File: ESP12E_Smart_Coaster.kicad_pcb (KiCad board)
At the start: 2 copper layers, 110.7 x 110.7 mm, 48 parts, among them J1 GPIO_Header, J2 SPI_Header, J3 MLX90614 Temp Sensor, J4 Programming_header, Q1 SI2302, SW1 SW_SPDT, SW2 SW_Push, U1 T6845C_Module, U2 AMS1117-3.3, U3 ESP-12E

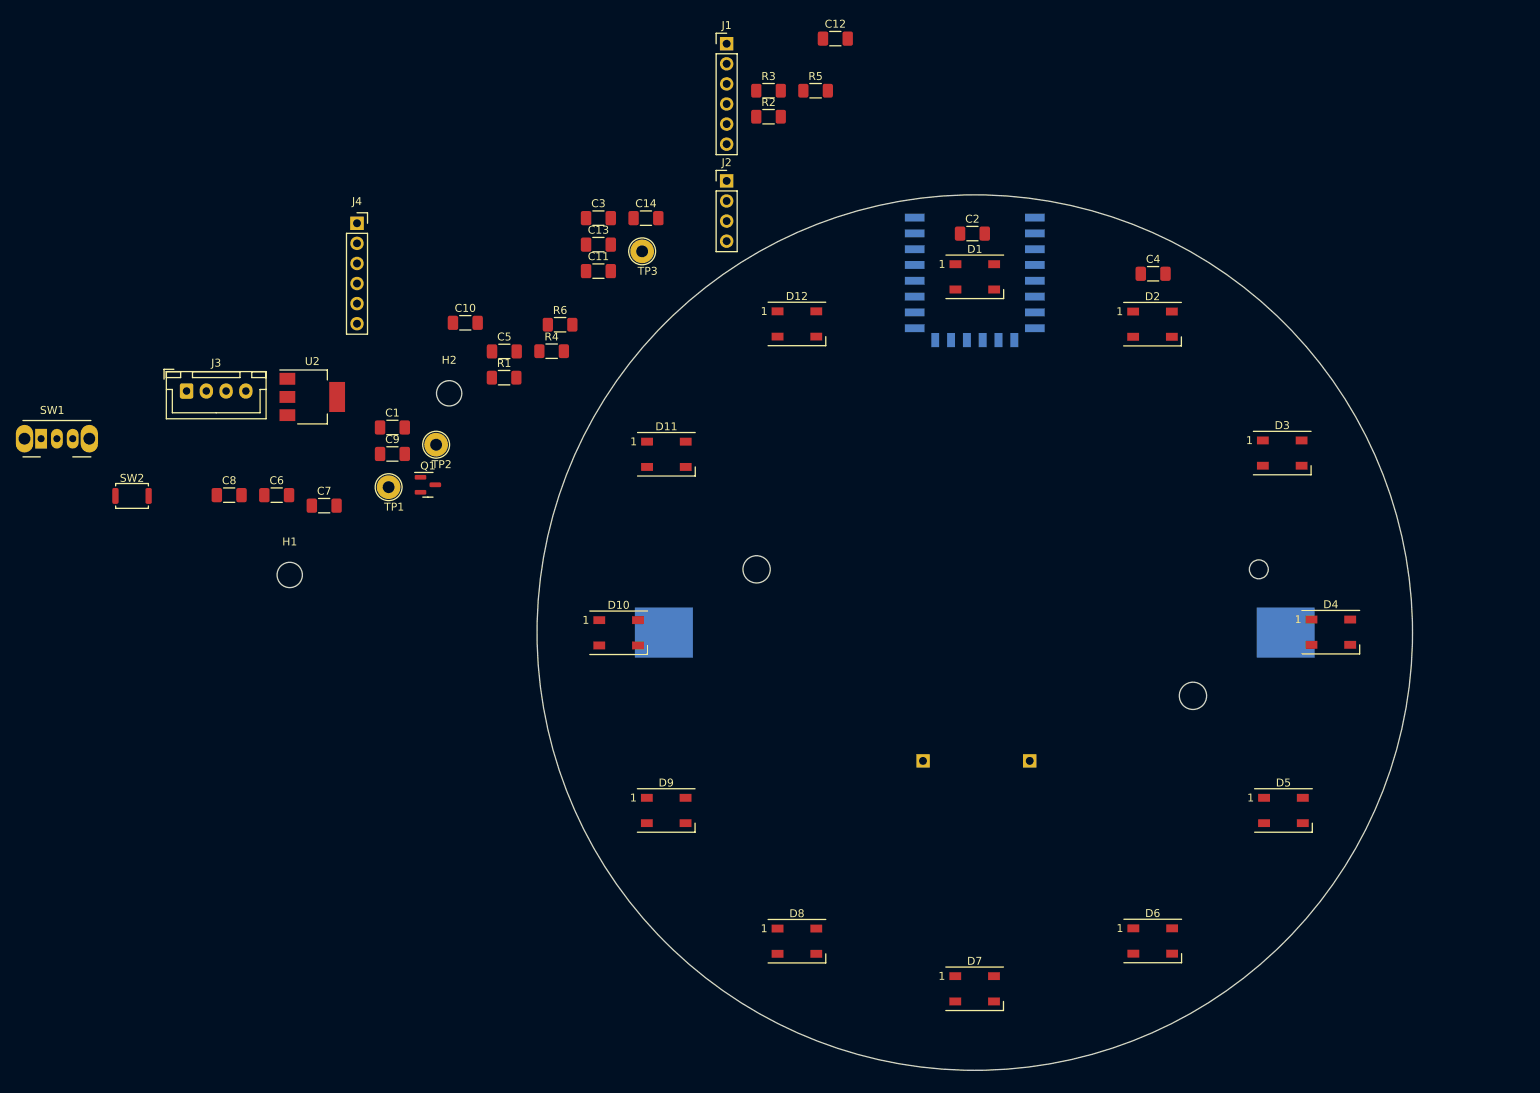
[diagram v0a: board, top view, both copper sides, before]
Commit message: re-arrange components but not completely done
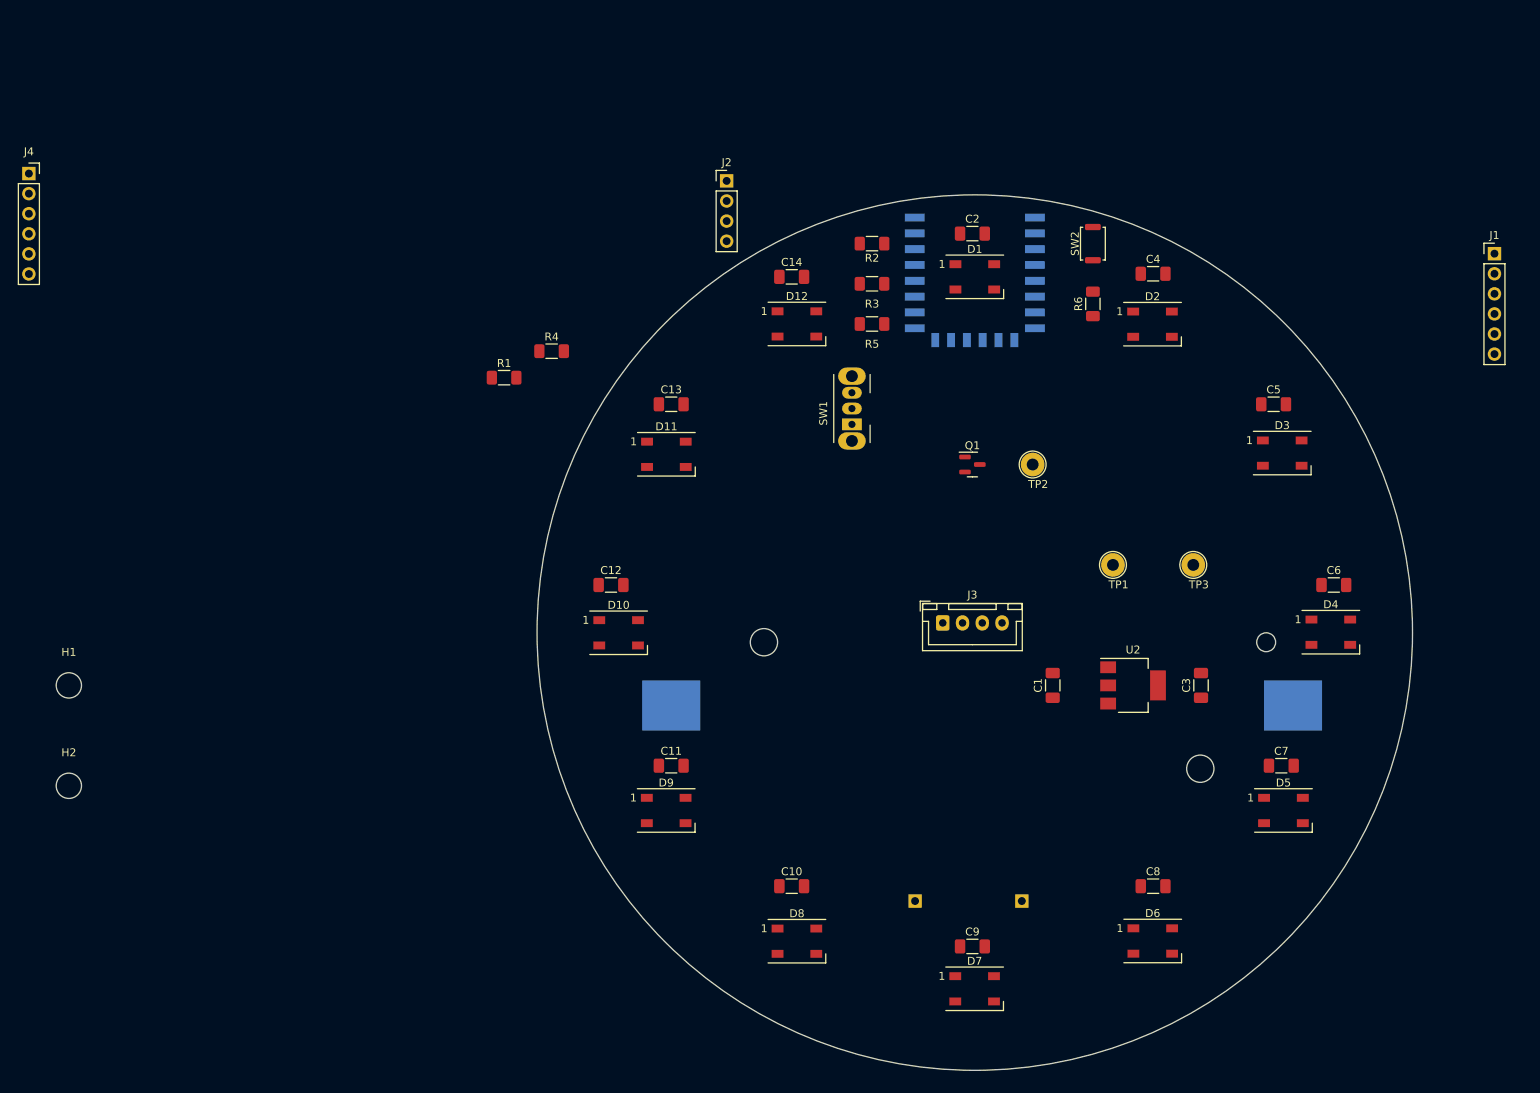
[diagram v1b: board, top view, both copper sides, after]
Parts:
- moved C6 134.2 mm to (185.4, 94.0)
- moved C8 126.9 mm to (162.6, 132.1)
- moved SW2 125.7 mm to (154.9, 50.8), turned to 90 degrees
- moved C7 125.5 mm to (178.8, 116.8)
- moved U2 110.1 mm to (160.0, 106.7)
- moved SW1 102.6 mm to (124.5, 73.7), turned to 90 degrees
- moved J1 100.7 mm to (205.7, 52.1)
- moved J3 100.1 mm to (135.9, 98.8)
- moved C5 97.5 mm to (177.8, 71.1)
- moved C3 96.5 mm to (168.6, 106.7), turned to 90 degrees
- moved C9 96.2 mm to (139.7, 139.7)
- moved TP1 92.2 mm to (157.5, 91.4)
- moved C1 89.7 mm to (149.9, 106.7), turned to 90 degrees
- moved C10 82.4 mm to (116.8, 132.1)
- moved TP3 80.2 mm to (167.6, 91.4)
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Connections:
- R3 pad 1: RESET -> (no net)
- R3 pad 2: GPIO2 -> (no net)

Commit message: Started PCB routing
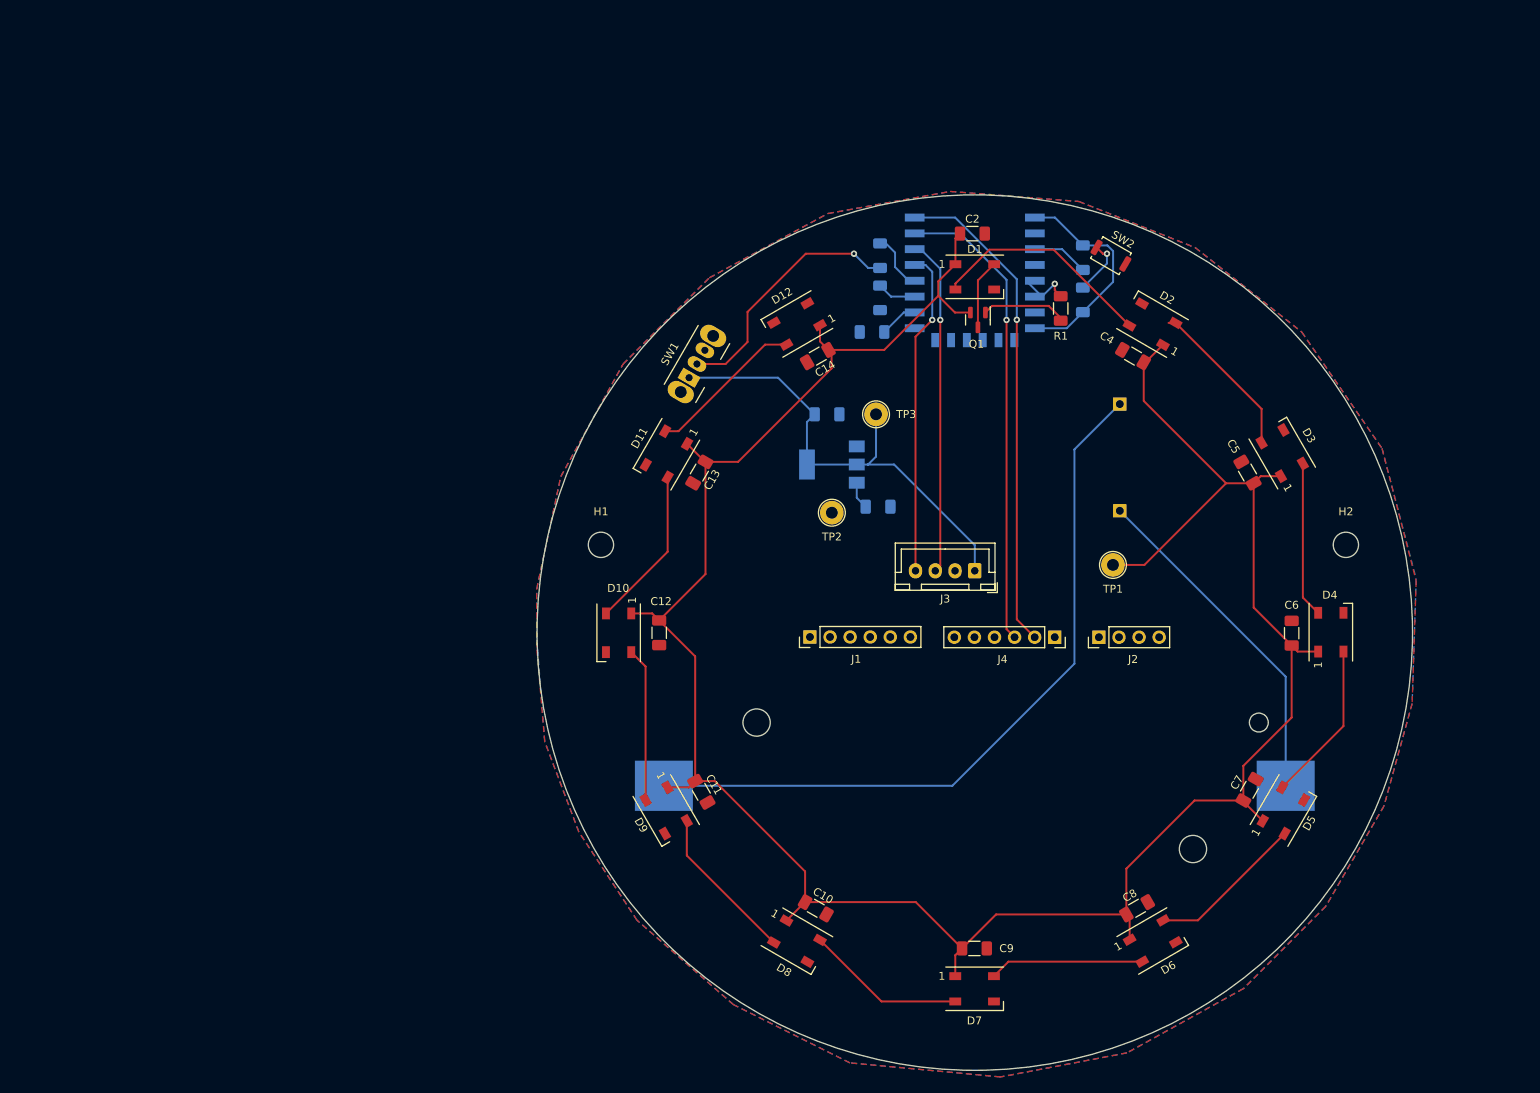
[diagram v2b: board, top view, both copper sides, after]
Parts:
- C1, C3, R2, R3, R4, R5, R6, U2: moved to B.Cu
- TP2: value 5V -> GND
- moved H2 164.4 mm to (186.9, 88.9)
- moved J4 142.4 mm to (150.1, 100.6), turned to -90 degrees
- moved J1 99.2 mm to (119.2, 100.6), turned to 90 degrees
- moved J2 74.5 mm to (155.7, 100.6), turned to 90 degrees
- moved R1 70.9 mm to (150.9, 59.0), turned to -90 degrees
- moved H1 69.6 mm to (92.7, 88.9)
- moved R4 68.2 mm to (153.7, 52.6), turned to -90 degrees
- moved C3 58.4 mm to (121.3, 72.4), turned to 0 degrees
- moved U1 48.0 mm to (148.8, 77.3), turned to 0 degrees
- moved U2 47.2 mm to (121.9, 78.7), turned to 180 degrees
- moved TP3 44.4 mm to (127.5, 72.4)
- moved C1 31.6 mm to (127.8, 84.1), turned to 0 degrees
- moved TP2 26.1 mm to (121.9, 84.8)
- moved SW1 21.4 mm to (103.9, 67.8), turned to 60 degrees
- moved Q1 18.3 mm to (140.4, 60.5), turned to -90 degrees
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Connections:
- R3 pad 1: (no net) -> RESET
- R3 pad 2: (no net) -> GPIO2
- TP2 pad 1: unconnected-(TP2-Pad1) -> GND
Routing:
- net +5V: track 0.00 -> 319.7 mm
- net Net-(BT1-Pad2): track 0.00 -> 93.6 mm
- net RESET: track 0.00 -> 88.2 mm
- net TXD: track 0.00 -> 62.4 mm, vias 0 -> 1
- net RXD: track 0.00 -> 59.7 mm, vias 0 -> 1
- net Net-(BT1-Pad1): track 0.00 -> 43.5 mm
- net SCL: track 0.00 -> 42.7 mm, vias 0 -> 1
- net SDA: track 0.00 -> 41.3 mm, vias 0 -> 1
- net Net-(R5-Pad1): track 0.00 -> 31.9 mm, vias 0 -> 1
- net Net-(D1-Pad2): track 0.00 -> 28.5 mm
- net Net-(D2-Pad2): track 0.00 -> 20.5 mm
- net Net-(D10-Pad2): track 0.00 -> 20.4 mm
- net Net-(D4-Pad2): track 0.00 -> 20.4 mm
- net Net-(D7-Pad2): track 0.00 -> 20.3 mm
- net Net-(D8-Pad2): track 0.00 -> 19.9 mm
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- added copper zone on B.Cu, net GND
- added copper zone on F.Cu, net GND

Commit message: Added power connector and wake jumper
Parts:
- added JP1: SolderJumper_2_Open, Connector_PinHeader_2.54mm:PinHeader_1x02_P2.54mm_Vertical, F.Cu at (114.0, 43.9)
- C2: value 0.1uF -> 10u
- C3: value 10u -> 0.1uF
- J1: value GPIO_Header -> SPI_Header; footprint Connector_PinHeader_2.54mm:PinHeader_1x06_P2.54mm_Vertical -> Connector_PinHeader_2.54mm:PinHeader_1x04_P2.54mm_Vertical
- J2: value SPI_Header -> MLX90614 Temp Sensor; footprint Connector_PinHeader_2.54mm:PinHeader_1x04_P2.54mm_Vertical -> Connector_JST:JST_XH_B4B-XH-A_1x04_P2.50mm_Vertical
- J3: value MLX90614 Temp Sensor -> Programming_header; footprint Connector_JST:JST_XH_B4B-XH-A_1x04_P2.50mm_Vertical -> Connector_PinSocket_2.54mm:PinSocket_1x06_P2.54mm_Vertical
- J4: value Programming_header -> Power_Input_Header; footprint Connector_PinSocket_2.54mm:PinSocket_1x06_P2.54mm_Vertical -> Connector_JST:JST_XH_B2B-XH-A_1x02_P2.50mm_Vertical
- moved H1 120.6 mm to (207.9, 53.2)
- moved J4 58.5 mm to (92.8, 88.9), turned to 90 degrees
- moved J3 29.2 mm to (163.6, 109.4), turned to -90 degrees
- moved J2 12.0 mm to (144.5, 96.3), turned to 180 degrees
- moved J1 3.19 mm to (122.0, 99.1)
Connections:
- C2 pad 1: +5V -> RESET
- C3 pad 1: RESET -> +5V
- J1 pad 1: ADC -> SCLK
- J1 pad 2: GPIO9 -> MOSI
- J1 pad 3: GPIO10 -> MISO
- J1 pad 4: GPIO13 -> CS0
- J2 pad 1: SCLK -> RESET
- J2 pad 2: MOSI -> GND
- J2 pad 3: MISO -> SCL
- J2 pad 4: CS0 -> SDA
- J3 pad 1: RESET -> unconnected-(J3-Pad1)
- J3 pad 2: GND -> TXD
- J3 pad 3: SCL -> RXD
- J3 pad 4: SDA -> unconnected-(J3-Pad4)
- J4 pad 1: unconnected-(J4-Pad1) -> +5V
- J4 pad 2: TXD -> GND
- U3 pad 11: GPIO9 -> unconnected-(U3-Pad11)
- U3 pad 12: GPIO10 -> unconnected-(U3-Pad12)
- U3 pad 2: ADC -> unconnected-(U3-Pad2)
- U3 pad 4: GPIO16 -> WAKE
- U3 pad 5: GPIO14 -> unconnected-(U3-Pad5)
- U3 pad 7: GPIO13 -> unconnected-(U3-Pad7)
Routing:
- net TXD: track 62.4 -> 21.3 mm
- net RXD: track 59.7 -> 19.1 mm
- net SDA: track 41.3 -> 8.67 mm
- net SCL: track 42.7 -> 10.7 mm
- net RESET: track 88.2 -> 67.3 mm

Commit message: routing changes
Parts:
- moved H1 131.5 mm to (91.4, 114.3)
- moved U1 53.3 mm to (99.1, 96.5)
- moved JP1 52.0 mm to (165.1, 53.3), turned to -120 degrees
- moved J3 50.5 mm to (170.4, 59.4), turned to 50 degrees
- moved J1 50.3 mm to (125.8, 149.2), turned to 80 degrees
- moved J4 7.69 mm to (94.0, 81.3), turned to 70 degrees
- moved J2 3.49 mm to (143.4, 99.6)
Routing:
- net CS0: track 0.00 -> 103.1 mm, vias 0 -> 2
- net MOSI: track 0.00 -> 101.7 mm, vias 0 -> 2
- net MISO: track 0.00 -> 101.4 mm, vias 0 -> 2
- net SCLK: track 0.00 -> 90.8 mm, vias 0 -> 2
- net RESET: track 67.3 -> 129.2 mm, vias 0 -> 4
- net Net-(BT1-Pad2): track 93.6 -> 32.4 mm
- net Net-(BT1-Pad1): track 43.5 -> 85.3 mm
- net SCL: track 10.7 -> 51.9 mm
- net SDA: track 8.67 -> 48.4 mm
- net RXD: track 19.1 -> 53.0 mm, vias 1 -> 2
- net TXD: track 21.3 -> 50.5 mm, vias 1 -> 2
- net WAKE: track 0.00 -> 23.9 mm, vias 0 -> 2
- net LED_DIN: track 7.36 -> 5.07 mm
